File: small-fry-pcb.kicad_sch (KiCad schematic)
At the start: 139 parts, among them U1 Pico

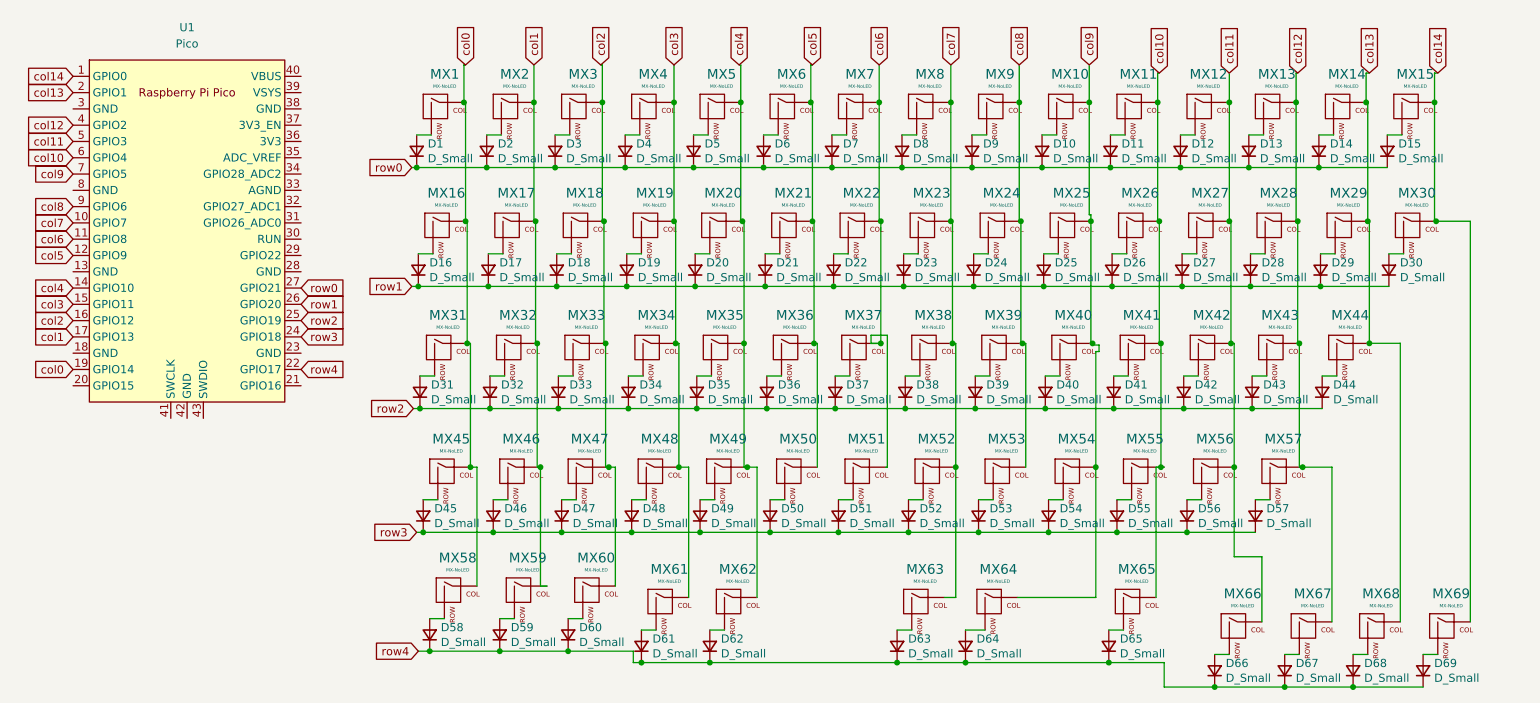
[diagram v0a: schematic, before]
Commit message: added extra switches
to accommodate the switch holes, leftmost diodes were moved and col routing was modified. extra pads connect back to the diodes.
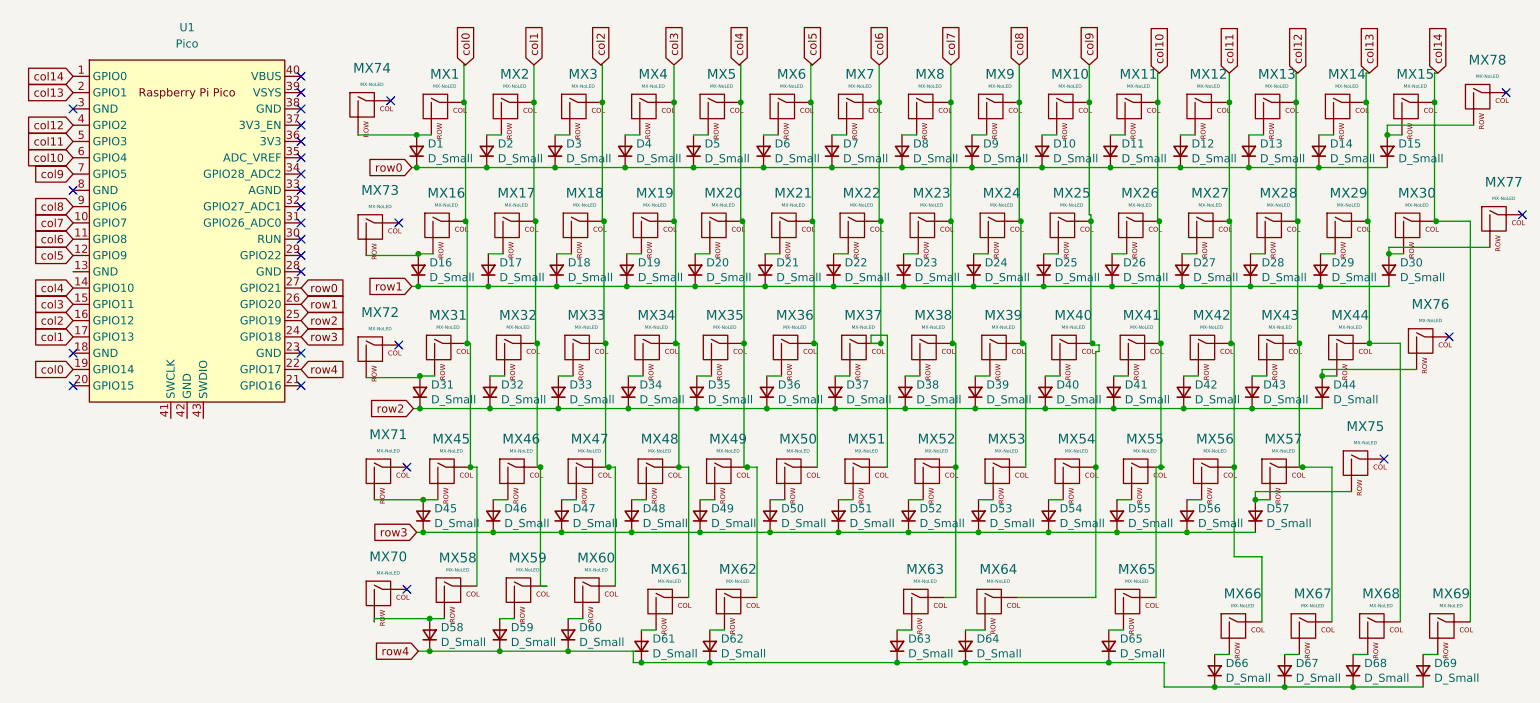
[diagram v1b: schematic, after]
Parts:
- added MX70, MX71, MX72, MX73, MX74, MX75, MX76, MX77, MX78: MX-NoLED, MX_Alps_Hybrid:MX-1.5U-NoLED, symbol MX_Alps_Hybrid:MX-NoLED
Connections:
- net at D1.2 (A), MX1.2 (ROW): now also MX74.2 (ROW)
- net at D15.2 (A), MX15.2 (ROW): now also MX78.2 (ROW)
- net at D16.2 (A), MX16.2 (ROW): now also MX73.2 (ROW)
- net at D30.2 (A), MX30.2 (ROW): now also MX77.2 (ROW)
- net at D31.2 (A), MX31.2 (ROW): now also MX72.2 (ROW)
- net at D44.2 (A), MX44.2 (ROW): now also MX76.2 (ROW)
- net at D45.2 (A), MX45.2 (ROW): now also MX71.2 (ROW)
- net at D57.2 (A), MX57.2 (ROW): now also MX75.2 (ROW)
- net at D58.2 (A), MX58.2 (ROW): now also MX70.2 (ROW)
- no-connect marks 0 -> 28
